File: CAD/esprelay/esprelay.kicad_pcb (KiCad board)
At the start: 2 copper layers, 65 x 20 mm, 42 parts, among them J1 Conn_01x06_Pin, J2 Conn_01x14_Pin, K1 G6K-2P-Y, K2 G6K-2P-Y, K3 G6K-2P-Y, Q1 Q_Photo_NPN, SW1 SW_SPST, U1 SPX3819M5-L-5-0, U2 SPX3819M5-L-3-3, U3 ESP-12F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

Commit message: Feat: Pretty much complete
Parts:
- removed R11: 10K, Resistor_SMD:R_0603_1608Metric
- moved R13 13.2 mm to (146.2, 89.8), turned to -90 degrees
- moved R12 11.7 mm to (144.7, 89.8), turned to -90 degrees
- moved R5 6.20 mm to (127.4, 80.2), turned to 180 degrees
- moved R7 6.06 mm to (131.2, 87.8)
- moved R4 5.54 mm to (127.4, 81.7), turned to 180 degrees
- moved R10 3.69 mm to (131.2, 83.3)
- moved R8 3.33 mm to (131.2, 86.3)
- moved R2 2.23 mm to (127.4, 83.2), turned to 180 degrees
- moved R9 1.81 mm to (131.2, 84.8)
- moved R3 1.78 mm to (127.4, 84.7)
- moved JP1 1.71 mm to (146.2, 86.8)
- moved SW1 1.70 mm to (130.5, 77.3)
- moved U5 1.51 mm to (138.4, 88.4)
- moved C3 1.35 mm to (127.4, 87.7)
- moved R1 1.35 mm to (127.4, 86.2)
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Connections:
- D1 pad 2: HRO1 -> RO1
- D2 pad 2: HRO2 -> RO2
- D3 pad 2: HRO3 -> RO3
- J2 pad 10: R2NC -> R2NO
- J2 pad 3: HPO45 -> HI1
- J2 pad 4: HI06 -> HI2
- J2 pad 5: HI07 -> HO1
- K1 pad 8: HRO1 -> RO1
- K2 pad 8: HRO2 -> RO2
- K3 pad 8: HRO3 -> RO3
- R10 pad 1: LPO4 -> GPIO5
- R12 pad 1: HI07 -> HI2
- R13 pad 1: HI06 -> HI1
- R7 pad 1: LRO1 -> GPIO13
- R8 pad 1: LRO2 -> GPIO12
- R9 pad 1: LR03 -> GPIO14
- U3 pad 16: LRO1 -> GPIO15
- U3 pad 19: LP45 -> GPIO4
- U3 pad 20: LI07 -> GPIO5
- U3 pad 5: LRO2 -> GPIO14
- U3 pad 6: LI06 -> GPIO12
- U3 pad 7: LR03 -> GPIO13
- U5 pad 1: LRO1 -> GPIO13
- U5 pad 10: LI07 -> GPIO15
- U5 pad 11: LI06 -> GPIO4
- U5 pad 12: HP45 -> RO3
- U5 pad 13: HP45 -> RO2
- U5 pad 14: HRO3 -> RO1
- U5 pad 15: HRO2 -> HO1
- U5 pad 16: HRO1 -> HO1
- U5 pad 2: LRO2 -> GPIO13
- U5 pad 3: LR03 -> GPIO12
- U5 pad 4: LP45 -> GPIO14
- U5 pad 5: LP45 -> GPIO5
- U5 pad 6: HI06 -> HI1
- U5 pad 7: HI07 -> HI2
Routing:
- net +3.3V: track 5.87 -> 86.6 mm, vias 0 -> 1
- net GPIO5: track 0.00 -> 43.6 mm, vias 0 -> 3
- net GPIO4: track 0.00 -> 32.7 mm, vias 0 -> 2
- net BOOT: track 0.00 -> 32.5 mm, vias 0 -> 3
- net GND: track 0.00 -> 29.5 mm, vias 0 -> 70
- net GPIO14: track 0.00 -> 28.9 mm, vias 0 -> 3
- net RST: track 0.00 -> 28.2 mm, vias 0 -> 3
- net HO1: track 0.00 -> 28.2 mm, vias 0 -> 2
- net GPIO15: track 0.00 -> 27.5 mm, vias 0 -> 2
- net HI1: track 0.00 -> 27.2 mm, vias 0 -> 2
- net GPIO12: track 0.00 -> 25.9 mm, vias 0 -> 3
- net GPIO13: track 0.00 -> 25.1 mm, vias 0 -> 3
- net HI2: track 0.00 -> 22.4 mm, vias 0 -> 2
- net PHOTO_OUT: track 0.00 -> 21.2 mm
- net RO3: track 0.00 -> 20.3 mm, vias 0 -> 1
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- added copper zone on B.Cu, net GND
- added copper zone on F.Cu, net GND
- added copper zone on B.Cu, net R1A
- added copper zone on F.Cu, net R1A
- added copper zone on B.Cu, net R1NC
- added copper zone on F.Cu, net R1NC

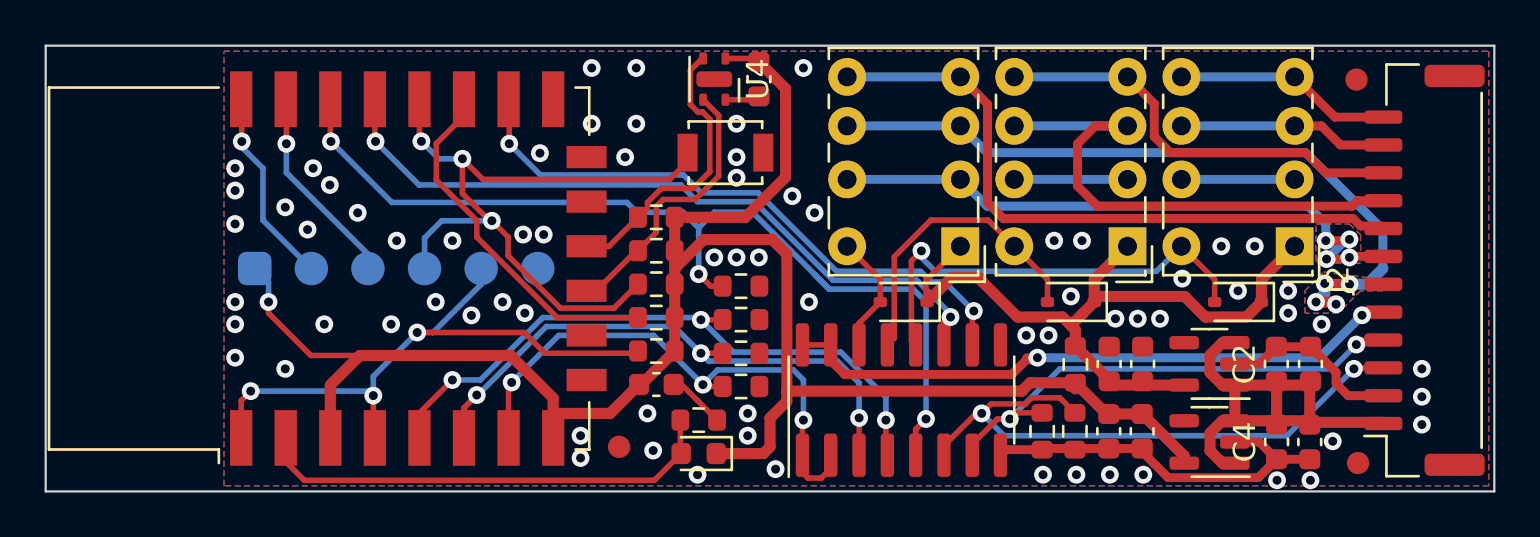
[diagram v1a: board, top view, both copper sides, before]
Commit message: Feat: Fixed lcsc product numbers
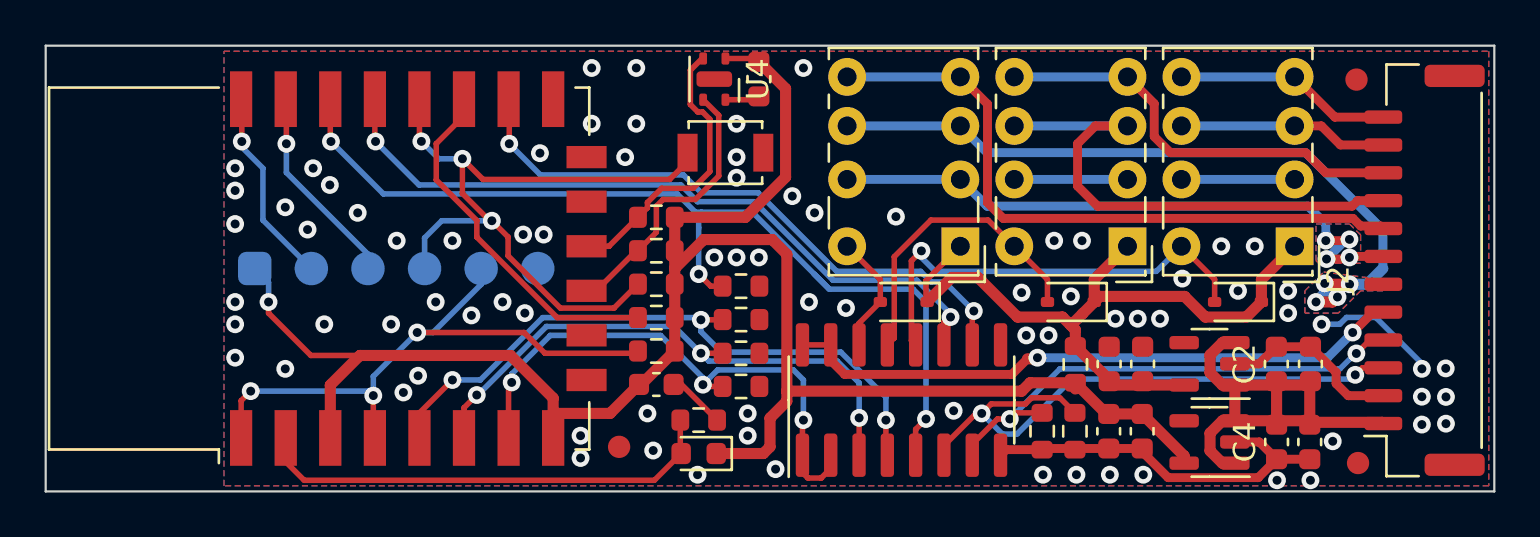
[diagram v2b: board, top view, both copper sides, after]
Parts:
- renumbered R12 to R11, R13 to R12
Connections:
- J2 pad MP: (no net) -> GND
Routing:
- net GND: track 29.5 -> 35.2 mm, vias 70 -> 79

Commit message: Feat: Finished silkscreen
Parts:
- added kibuzzard-65666C6B: G***, kibuzzard-65666C6B, B.Cu at (162.1, 91.0)
- added kibuzzard-65666C71: G***, kibuzzard-65666C71, B.Cu at (162.1, 89.4)
- added kibuzzard-65666C76: G***, kibuzzard-65666C76, B.Cu at (162.1, 87.9)
- added kibuzzard-65666C7B: G***, kibuzzard-65666C7B, B.Cu at (162.1, 86.4)
- added kibuzzard-65666C87: G***, kibuzzard-65666C87, B.Cu at (162.1, 84.8)
- added kibuzzard-65666CB0: G***, kibuzzard-65666CB0, B.Cu at (162.1, 83.3)
- added kibuzzard-65666CB7: G***, kibuzzard-65666CB7, B.Cu at (162.1, 81.7)
- added kibuzzard-65666CF7: G***, kibuzzard-65666CF7, B.Cu at (162.1, 80.2)
- added kibuzzard-65666CFD: G***, kibuzzard-65666CFD, B.Cu at (162.1, 78.6)
- added kibuzzard-65666D06: G***, kibuzzard-65666D06, B.Cu at (162.1, 77.1)
- added kibuzzard-65666D10: G***, kibuzzard-65666D10, B.Cu at (162.1, 75.5)
- added kibuzzard-65666D19: G***, kibuzzard-65666D19, B.Cu at (162.1, 74.0)
- added kibuzzard-6566713E: G***, kibuzzard-6566713E, B.Cu at (124.5, 90.3)
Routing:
- net GND: track 35.2 -> 54.3 mm
- net R1A: track 32.7 -> 34.2 mm
- net GPIO5: track 43.7 -> 42.8 mm
- net (no net): vias 1 -> 0
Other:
- board text added: "3v3"
- board text added: "boot"
- board text added: "gnd"
- board text added: "rst"
- board text added: "rxd"
- board text added: "txd"
